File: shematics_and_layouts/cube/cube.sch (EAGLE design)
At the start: 13 parts, among them X1 LEDs, X2 BAT

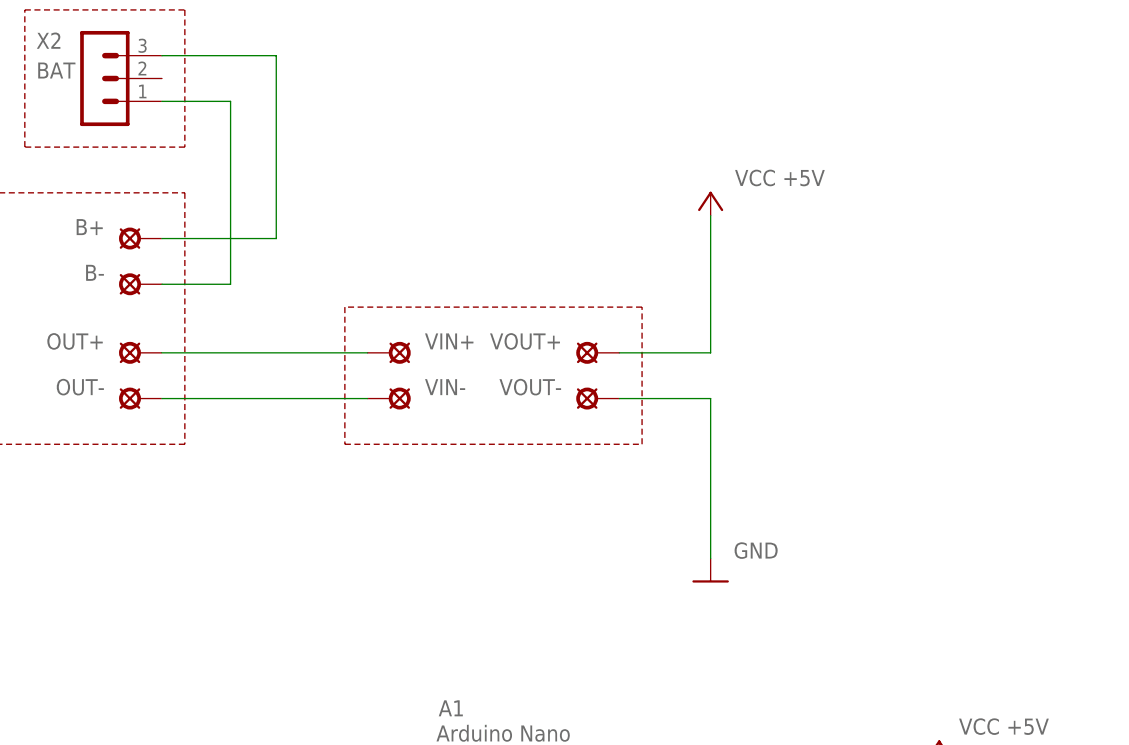
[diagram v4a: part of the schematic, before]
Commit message: TASK: Add switch to cube
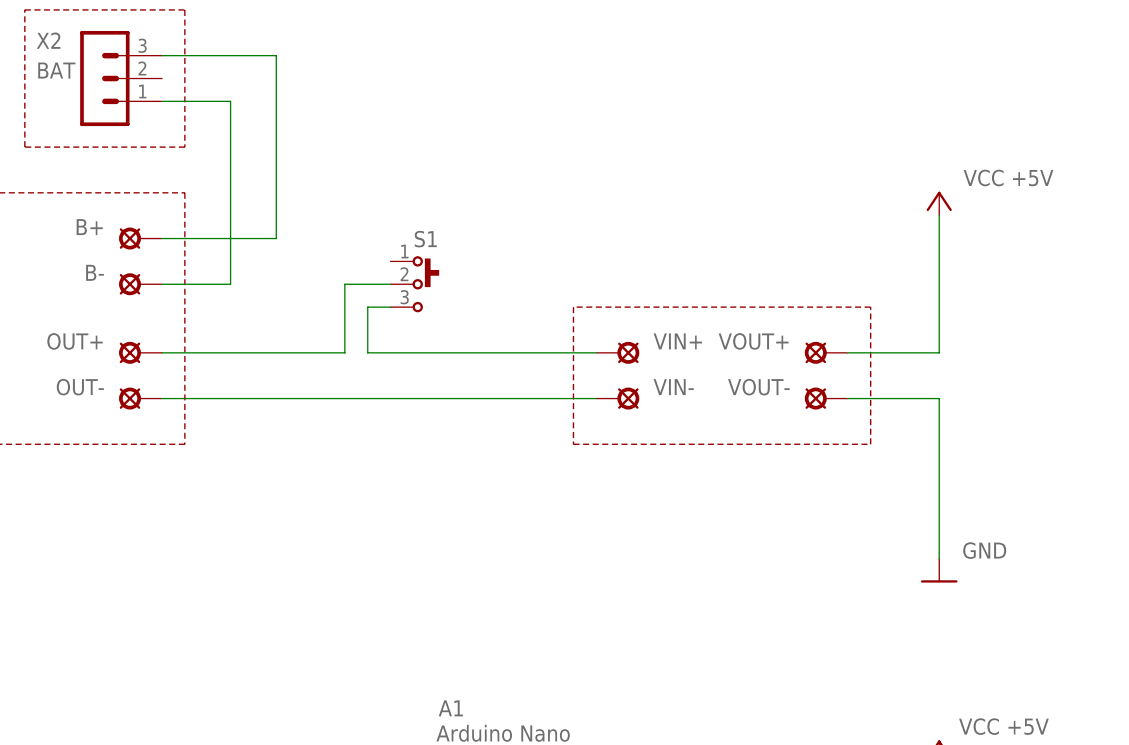
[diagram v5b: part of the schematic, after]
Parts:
- added S1: EG1218, switch-e-switch:EG1218
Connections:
- new net N$3: S1.3, VIN+.MP
- net N$1: now also S1.2; no longer VIN+.MP
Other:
- moved on the sheet: VIN+, VIN-, VOUT+, VOUT-
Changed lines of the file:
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@@
 <layer number="48" name="Document" color="7" fill="1" visible="no" active="no"/>
 <layer number="49" name="Reference" color="7" fill="1" visible="no" active="no"/>
+<layer number="50" name="dxf" color="7" fill="1" visible="no" active="no"/>
 <layer number="51" name="tDocu" color="7" fill="1" visible="no" active="no"/>
 <layer number="52" name="bDocu" color="7" fill="1" visible="no" active="no"/>
+<layer number="53" name="tGND_GNDA" color="7" fill="1" visible="no" active="no"/>
+<layer number="54" name="bGND_GNDA" color="7" fill="1" visible="no" active="no"/>
+<layer number="56" name="wert" color="7" fill="1" visible="no" active="no"/>
 <layer number="90" name="Modules" color="5" fill="1" visible="yes" active="yes"/>
 <layer number="91" name="Nets" color="2" fill="1" visible="yes" active="yes"/>
@@
 <layer number="97" name="Info" color="7" fill="1" visible="yes" active="yes"/>
 <layer number="98" name="Guide" color="6" fill="1" visible="yes" active="yes"/>
+<layer number="99" name="SpiceOrder" color="7" fill="1" visible="yes" active="yes"/>
+<layer number="100" name="Mechanical" color="7" fill="1" visible="yes" active="yes"/>
+<layer number="101" name="Gehäuse" color="7" fill="1" visible="yes" active="yes"/>
+<layer number="102" name="ID" color="7" fill="1" visible="yes" active="yes"/>
+<layer number="103" name="tMap" color="7" fill="1" visible="yes" active="yes"/>
+<layer number="104" name="bMap" color="7" fill="1" visible="yes" active="yes"/>
+<layer number="105" name="tPlate" color="7" fill="1" visible="yes" active="yes"/>
+<layer number="106" name="bPlate" color="7" fill="1" visible="yes" active="yes"/>
+<layer number="107" name="Crop" color="7" fill="1" visible="yes" active="yes"/>
+<layer number="111" name="tGTest" color="7" fill="1" visible="yes" active="yes"/>
+<layer number="112" name="bGTest" color="7" fill="1" visible="yes" active="yes"/>
+<layer number="116" name="Patch_BOT" color="7" fill="1" visible="yes" active="yes"/>
+<layer number="150" name="Notes" color="7" fill="1" visible="yes" active="yes"/>
+<layer number="151" name="HeatSink" color="7" fill="1" visible="yes" active="yes"/>
+<layer number="199" name="EXTD_ERC" color="7" fill="1" visible="yes" active="yes"/>
+<layer number="200" name="200bmp" color="7" fill="1" visible="yes" active="yes"/>
+<layer number="201" name="201bmp" color="7" fill="1" visible="yes" active="yes"/>
+<layer number="250" name="Descript" color="7" fill="1" visible="yes" active="yes"/>
+<layer number="251" name="SMDround" color="7" fill="1" visible="yes" active="yes"/>
+<layer number="254" name="cooling" color="7" fill="1" visible="yes" active="yes"/>
 </layers>
 <schematic xreflabel="%F%N/%S.%C%R" xrefpart="/%S.%C%R">
@@
 <part name="GND5" library="supply1" deviceset="GND" device=""/>
 <part name="X2" library="con-lstb" deviceset="MA03-1" device="" value="BAT"/>
+<part name="S1" library="switch-e-switch" deviceset="EG1218" device="" value=""/>
 </parts>
 <sheets>
 <sheet>
 <plain>
-<wire x1="-38.1" y1="124.46" x2="-38.1" y2="109.22" width="0.1524" layer="94" style="dashdot"/>
-<wire x1="-38.1" y1="109.22" x2="-5.08" y2="109.22" width="0.1524" layer="94" style="dashdot"/>
-<wire x1="-5.08" y1="109.22" x2="-5.08" y2="124.46" width="0.1524" layer="94" style="dashdot"/>
-<wire x1="-5.08" y1="124.46" x2="-38.1" y2="124.46" width="0.1524" layer="94" style="dashdot"/>
+<wire x1="-12.7" y1="124.46" x2="-12.7" y2="109.22" width="0.1524" layer="94" style="dashdot"/>
+<wire x1="-12.7" y1="109.22" x2="20.32" y2="109.22" width="0.1524" layer="94" style="dashdot"/>
+<wire x1="20.32" y1="109.22" x2="20.32" y2="124.46" width="0.1524" layer="94" style="dashdot"/>
+<wire x1="20.32" y1="124.46" x2="-12.7" y2="124.46" width="0.1524" layer="94" style="dashdot"/>
 <wire x1="-55.88" y1="137.16" x2="-55.88" y2="109.22" width="0.1524" layer="94" style="dashdot"/>
 <wire x1="-55.88" y1="109.22" x2="-91.44" y2="109.22" width="0.1524" layer="94" style="dashdot"/>
@@
 <instances>
 <instance part="A1" gate="G$1" x="-15.24" y="55.88" smashed="yes"/>
-<instance part="VOUT+" gate="G$1" x="-10.16" y="119.38" smashed="yes" rot="R90">
-<attribute name="NAME" x="-13.97" y="121.539" size="1.778" layer="95" rot="R180"/>
-</instance>
-<instance part="VOUT-" gate="G$1" x="-10.16" y="114.3" smashed="yes" rot="R90">
-<attribute name="NAME" x="-13.97" y="116.459" size="1.778" layer="95" rot="R180"/>
-</instance>
-<instance part="VIN+" gate="G$1" x="-33.02" y="119.38" smashed="yes" rot="R270">
-<attribute name="NAME" x="-29.21" y="119.761" size="1.778" layer="95"/>
-</instance>
-<instance part="VIN-" gate="G$1" x="-33.02" y="114.3" smashed="yes" rot="R270">
-<attribute name="NAME" x="-29.21" y="114.681" size="1.778" layer="95"/>
-</instance>
-<instance part="GND2" gate="1" x="2.54" y="93.98" smashed="yes">
-<attribute name="VALUE" x="5.08" y="96.52" size="1.778" layer="96"/>
-</instance>
-<instance part="P+1" gate="VCC" x="2.54" y="137.16" smashed="yes">
-<attribute name="VALUE" x="15.24" y="139.7" size="1.778" layer="96" rot="R180"/>
+<instance part="VOUT+" gate="G$1" x="15.24" y="119.38" smashed="yes" rot="R90">
+<attribute name="NAME" x="11.43" y="121.539" size="1.778" layer="95" rot="R180"/>
+</instance>
+<instance part="VOUT-" gate="G$1" x="15.24" y="114.3" smashed="yes" rot="R90">
+<attribute name="NAME" x="11.43" y="116.459" size="1.778" layer="95" rot="R180"/>
+</instance>
+<instance part="VIN+" gate="G$1" x="-7.62" y="119.38" smashed="yes" rot="R270">
+<attribute name="NAME" x="-3.81" y="119.761" size="1.778" layer="95"/>
+</instance>
+<instance part="VIN-" gate="G$1" x="-7.62" y="114.3" smashed="yes" rot="R270">
+<attribute name="NAME" x="-3.81" y="114.681" size="1.778" layer="95"/>
+</instance>
+<instance part="GND2" gate="1" x="27.94" y="93.98" smashed="yes">
+<attribute name="VALUE" x="30.48" y="96.52" size="1.778" layer="96"/>
+</instance>
+<instance part="P+1" gate="VCC" x="27.94" y="137.16" smashed="yes">
+<attribute name="VALUE" x="40.64" y="139.7" size="1.778" layer="96" rot="R180"/>
 </instance>
 <instance part="P+2" gate="VCC" x="-60.96" y="48.26" smashed="yes">
@@
 <attribute name="NAME" x="-72.39" y="153.162" size="1.778" layer="95"/>
 </instance>
+<instance part="S1" gate="G$1" x="-30.48" y="127"/>
 </instances>
 <busses>
@@
 <segment>
 <pinref part="VOUT-" gate="G$1" pin="MP"/>
-<wire x1="-7.62" y1="114.3" x2="2.54" y2="114.3" width="0.1524" layer="91"/>
-<wire x1="2.54" y1="114.3" x2="2.54" y2="96.52" width="0.1524" layer="91"/>
+<wire x1="17.78" y1="114.3" x2="27.94" y2="114.3" width="0.1524" layer="91"/>
+<wire x1="27.94" y1="114.3" x2="27.94" y2="96.52" width="0.1524" layer="91"/>
 <pinref part="GND2" gate="1" pin="GND"/>
 </segment>
@@
 <segment>
 <pinref part="P+1" gate="VCC" pin="VCC"/>
-<wire x1="2.54" y1="134.62" x2="2.54" y2="119.38" width="0.1524" layer="91"/>
+<wire x1="27.94" y1="134.62" x2="27.94" y2="119.38" width="0.1524" layer="91"/>
 <pinref part="VOUT+" gate="G$1" pin="MP"/>
-<wire x1="-7.62" y1="119.38" x2="2.54" y2="119.38" width="0.1524" layer="91"/>
+<wire x1="17.78" y1="119.38" x2="27.94" y2="119.38" width="0.1524" layer="91"/>
 </segment>
 <segment>
@@
 </segment>
 </net>
-<net name="N$1" class="0">
-<segment>
-<pinref part="OUT+" gate="G$1" pin="MP"/>
-<pinref part="VIN+" gate="G$1" pin="MP"/>
-<wire x1="-58.42" y1="119.38" x2="-35.56" y2="119.38" width="0.1524" layer="91"/>
-</segment>
-</net>
 <net name="N$2" class="0">
 <segment>
 <pinref part="OUT-" gate="G$1" pin="MP"/>
-<wire x1="-58.42" y1="114.3" x2="-35.56" y2="114.3" width="0.1524" layer="91"/>
+<wire x1="-58.42" y1="114.3" x2="-10.16" y2="114.3" width="0.1524" layer="91"/>
 <pinref part="VIN-" gate="G$1" pin="MP"/>
 </segment>
@@
 </segment>
 </net>
+<net name="N$1" class="0">
+<segment>
+<pinref part="OUT+" gate="G$1" pin="MP"/>
+<wire x1="-58.42" y1="119.38" x2="-38.1" y2="119.38" width="0.1524" layer="91"/>
+<wire x1="-38.1" y1="119.38" x2="-38.1" y2="127" width="0.1524" layer="91"/>
+<pinref part="S1" gate="G$1" pin="2"/>
+<wire x1="-38.1" y1="127" x2="-33.02" y2="127" width="0.1524" layer="91"/>
+</segment>
+</net>
+<net name="N$3" class="0">
+<segment>
+<pinref part="S1" gate="G$1" pin="3"/>
+<wire x1="-33.02" y1="124.46" x2="-35.56" y2="124.46" width="0.1524" layer="91"/>
+<wire x1="-35.56" y1="124.46" x2="-35.56" y2="119.38" width="0.1524" layer="91"/>
+<pinref part="VIN+" gate="G$1" pin="MP"/>
+<wire x1="-35.56" y1="119.38" x2="-10.16" y2="119.38" width="0.1524" layer="91"/>
+</segment>
+</net>
